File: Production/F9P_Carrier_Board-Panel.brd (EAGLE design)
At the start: 154.9 x 146.3 mm, 666 parts, among them J11 MICROMOD-2222-C, J13 U.FL, J14 QWIIC_RIGHT_ANGLE, J17 JTAG, J20 MICROMOD-2222-C, J22 U.FL, J23 QWIIC_RIGHT_ANGLE, J26 JTAG, J29 MICROMOD-2222-C, J31 U.FL, J32 QWIIC_RIGHT_ANGLE, J35 JTAG, J4 U.FL, J5 QWIIC_RIGHT_ANGLE, J6 MICROMOD-2222-C, J8 JTAG, U1 U-BLOX_ZED-F9P, U2 AP7361C-33, U3 U-BLOX_ZED-F9P, U4 AP7361C-33, U5 AP7361C-33, U6 U-BLOX_ZED-F9P, U7 AP7361C-33, U8 U-BLOX_ZED-F9P

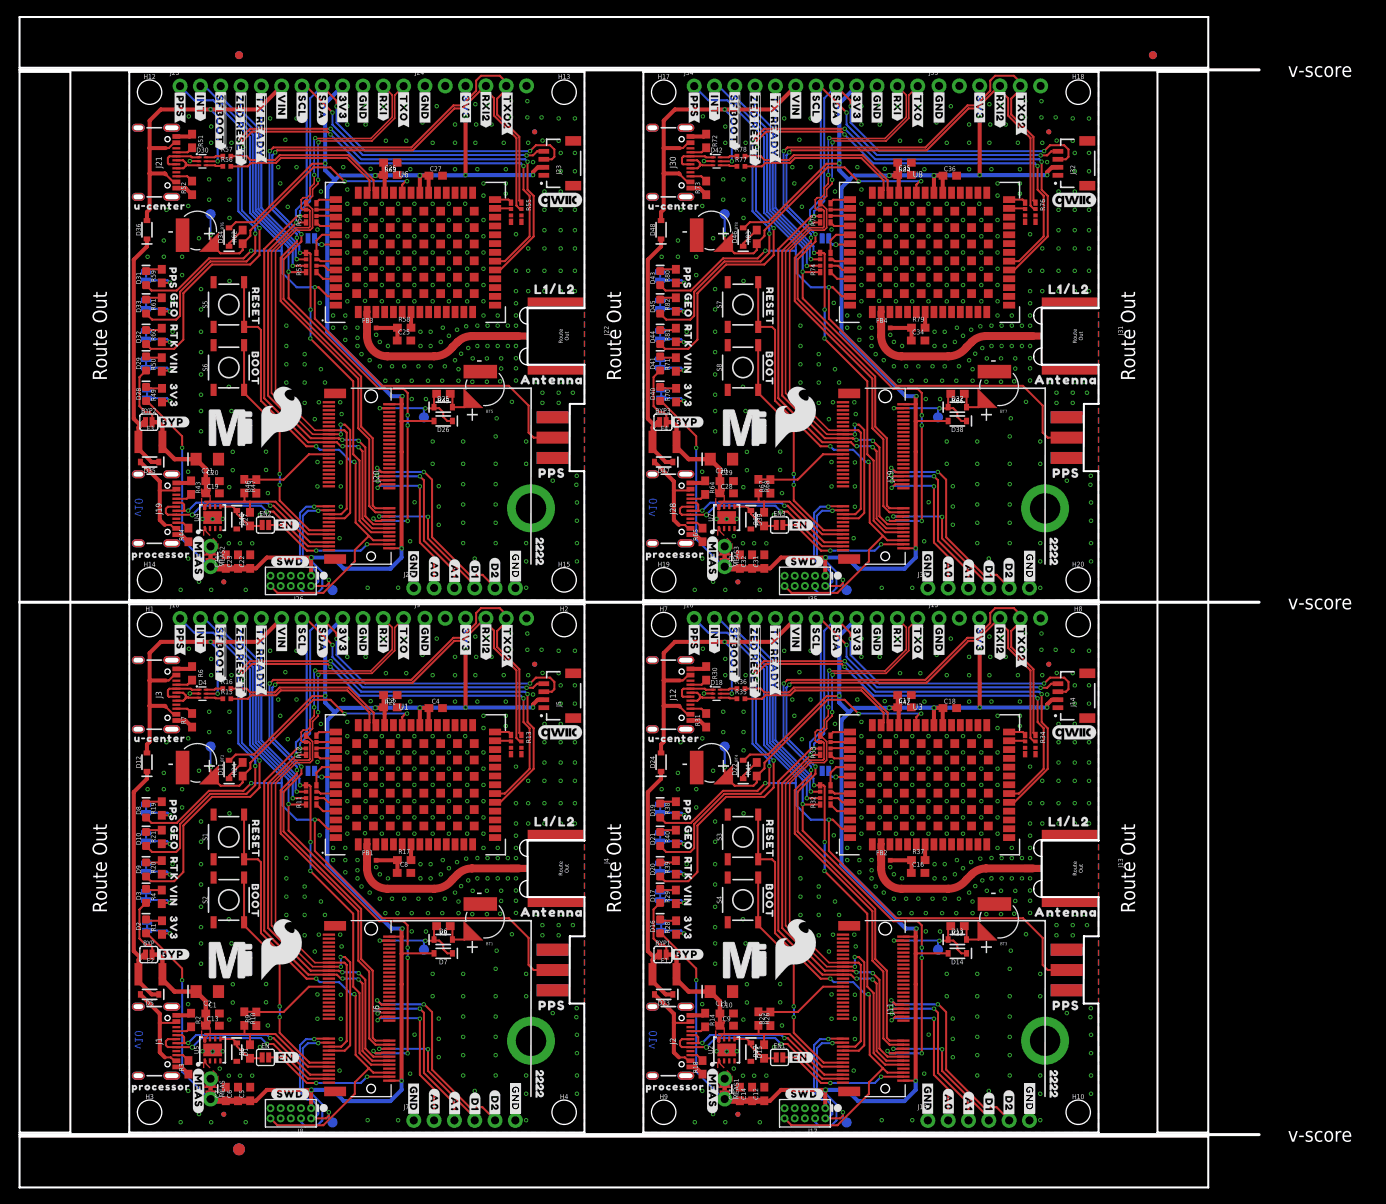
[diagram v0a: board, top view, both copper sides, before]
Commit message: Removes GPS silk, adds GNSS silk, repanelizes with new silk
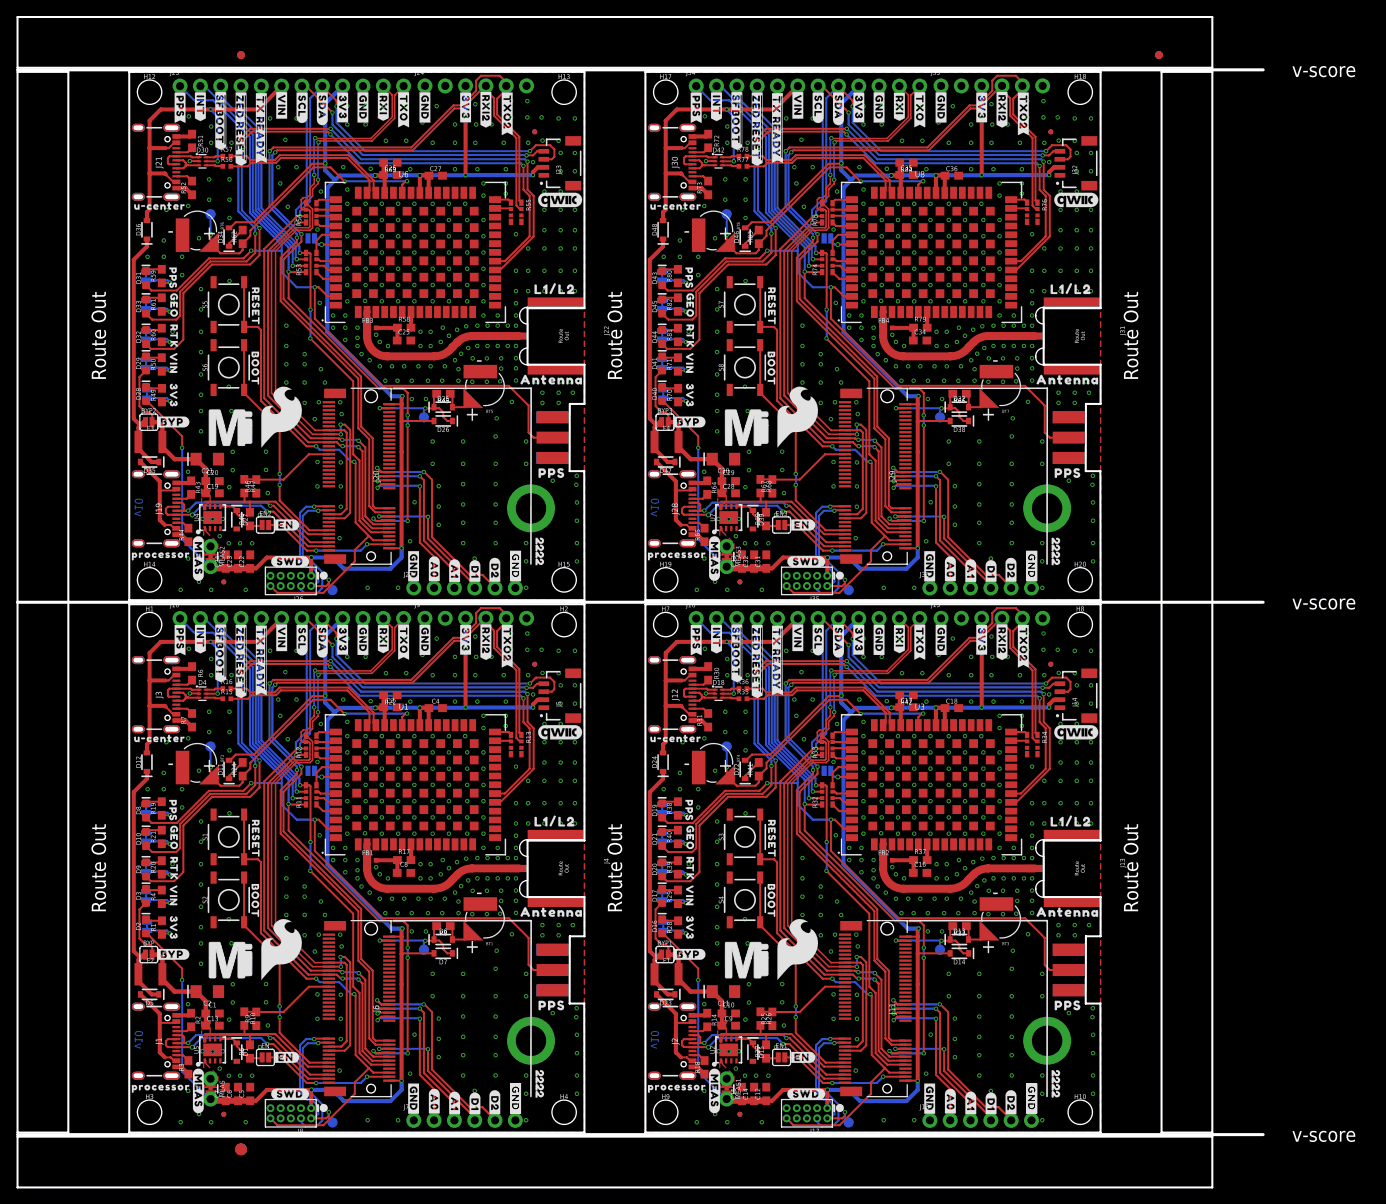
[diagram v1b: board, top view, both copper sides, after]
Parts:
- U$120, U$206, U$288: device top:GPS19 -> top:U#CENTER20
- U$121, U$207, U$289: device top:U#CENTER20 -> SparkFun-Aesthetics:QWIIC_5.5MM
- U$122, U$208, U$290: device SparkFun-Aesthetics:QWIIC_5.5MM -> bot:#SCL#1
- U$123, U$209, U$291: device bot:#SCL#1 -> bot:#SDA#0
- U$124, U$210, U$292: device bot:#SDA#0 -> bot:#TXO#5
- U$125, U$211, U$293: device bot:#TXO#5 -> bot:#RXI#6
- U$126, U$212, U$294: device bot:#RXI#6 -> top:PPS15
- U$127, U$213, U$295: device top:PPS15 -> top:ANTENNA16
- U$128, U$214, U$296: device top:ANTENNA16 -> top:L1#L216
- U$129, U$215, U$297: device top:L1#L216 -> top:##CS##9
- U$130, U$216, U$298: device top:##CS##9 -> top:#CLK#7
- U$135, U$217, U$299: device top:#CLK#7 -> top:#SDO#9
- U$136, U$218, U$300: device top:#SDO#9 -> top:#SDI#11
- U$137, U$219, U$301: device top:#SDI#11 -> top:BLUETOOTH24
- U$138, U$220, U$302: device top:BLUETOOTH24 -> top:U#CENTER22
- U$139, U$221, U$303: device top:U#CENTER22 -> top:L1#L217
- U$140, U$222, U$304: device top:L1#L217 -> top:ANTENNA17
- U$141, U$223, U$305: device top:ANTENNA17 -> top:PPS16
- U$142, U$224, U$306: device top:PPS16 -> bot:##ZED_RESET##9
- U$143, U$225, U$307: device bot:##ZED_RESET##9 -> top:##ZED_RESET##14
- U$144, U$226, U$308: device top:##ZED_RESET##14 -> top:##SFBOOT##13
- U$145, U$227, U$309: device top:##SFBOOT##13 -> bot:##SFBOOT##8
- U$146, U$228, U$310: device bot:##SFBOOT##8 -> SparkFun-MicroMod:MICROMOD_LOGO_.5
- U$147, U$229, U$311: device SparkFun-MicroMod:MICROMOD_LOGO_.5 -> SparkFun-MicroMod:MICROMOD_MI_LOGO_1
- U$148, U$230, U$312: device SparkFun-MicroMod:MICROMOD_MI_LOGO_1 -> SparkFun-Aesthetics:SFE_LOGO_FLAME_.3
- U$149, U$231, U$313: device SparkFun-Aesthetics:SFE_LOGO_FLAME_.3 -> top:#GND#0
- U$152, U$234, U$316: device top:#GND#0 -> top:#A0#8
- U$153, U$235, U$317: device top:#A0#8 -> top:#A1#8
- U$154, U$236, U$318: device top:#A1#8 -> top:#D1#8
- U$155, U$237, U$319: device top:#D1#8 -> top:#D2#8
- U$156, U$238, U$320: device top:#D2#8 -> top:PROCESSOR23
- U$158, U$240, U$322: device top:PROCESSOR23 -> bot:#A0#14
- U$159, U$241, U$323: device bot:#A0#14 -> bot:#A1#14
- U$160, U$242, U$324: device bot:#A1#14 -> bot:#D1#14
- U$161, U$243, U$325: device bot:#D1#14 -> bot:#D2#14
- U$162, U$244, U$326: device bot:#D2#14 -> top:#GND#0
- U$164, U$246, U$328: device top:#GND#0 -> top:GNSS21
- U$45: device top:GPS19 -> top:GNSS21
- moved U$224 54.7 mm to (14.0, 125.6), flipped to the top, turned to 270 degrees
- moved U$142 54.5 mm to (78.5, 59.1), flipped to the top, turned to 270 degrees
- moved U$306 54.5 mm to (78.5, 125.6), flipped to the top, turned to 270 degrees
- moved U$139 53.0 mm to (117.5, 38.2), turned to 0 degrees
- moved U$303 53.0 mm to (117.5, 104.8), turned to 0 degrees
- moved U$221 52.7 mm to (53.0, 104.8), turned to 0 degrees
- moved U$126 50.7 mm to (117.3, 15.9), turned to 0 degrees
- moved U$294 50.7 mm to (117.3, 82.4), turned to 0 degrees
- moved U$212 50.6 mm to (52.8, 82.4), turned to 0 degrees
- moved U$121 50.3 mm to (118.4, 50.0)
- moved U$289 50.3 mm to (118.4, 116.6)
- moved U$207 50.0 mm to (53.8, 116.6)
- moved U$238 41.8 mm to (3.96, 72.3), turned to 0 degrees
- moved U$156 41.5 mm to (68.5, 5.74), turned to 0 degrees
- moved U$320 41.5 mm to (68.5, 72.3), turned to 0 degrees
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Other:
- board size 154.9 x 146.3 mm -> 155.7 x 146.3 mm

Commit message: Updated panel
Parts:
- added D49: 0.5A/40V/420mV, SparkFun-DiscreteSemi:SOD-323
- added D50, D51: 3A/10V/280mV, SparkFun-DiscreteSemi:SOD-323
- added D52: PESD0402, SparkFun-DiscreteSemi:0402
- added U$329: (no value), bot:##SFBOOT##8
- added U$330: (no value), SparkFun-MicroMod:MICROMOD_LOGO_.5
- added U$331: (no value), SparkFun-MicroMod:MICROMOD_MI_LOGO_1
- added U$332: (no value), SparkFun-Aesthetics:SFE_LOGO_FLAME_.3
- added U$333, U$334, U$335, U$346, U$347: (no value), top:#GND#0
- added U$336: (no value), top:#A0#8
- added U$337: (no value), top:#A1#8
- added U$338: (no value), top:#D1#8
- added U$339: (no value), top:#D2#8
- added U$340, U$341: (no value), top:PROCESSOR23
- added U$342: (no value), bot:#A0#14
- added U$343: (no value), bot:#A1#14
- added U$344: (no value), bot:#D1#14
- added U$345: (no value), bot:#D2#14
- added U$348: (no value), top:GNSS21
- added U$349: (no value), top:GNSS501
- added U$350: (no value), top:CARRIER502
- added U$351: (no value), top:BOARD503
- added U$352: (no value), top:2222501
- added U$353, U$354: (no value), top:#NC#4
- added U$355, U$356: (no value), top:#NC#5
- D13: value 3A/10V/280mV -> PESD0402; device SparkFun-DiscreteSemi:SOD-323 -> SparkFun-DiscreteSemi:0402
- D14, D38: value 1A/23V/620mV -> 3A/10V/280mV
- D15: value 3.3V -> 1A/23V/620mV
- D16, D29: value RED -> 3.3V; device SparkFun-LED:LED-0603 -> SparkFun-DiscreteSemi:SOD-323
- D18, D30: value PRTR5V0U2F -> RED; device SparkFun-IC-Power:SOT886 -> SparkFun-LED:LED-0603
- D19, D32, D45: value BLUE -> PRTR5V0U2F; device SparkFun-LED:LED-0603 -> SparkFun-IC-Power:SOT886
- D22, D34, D46: value 0.5A/40V/420mV -> BLUE; device SparkFun-DiscreteSemi:SOD-323 -> SparkFun-LED:LED-0603
- D23, D36: value 3A/10V/280mV -> 0.5A/40V/420mV
- D26: value 1A/23V/620mV -> PESD0402; device SparkFun-DiscreteSemi:SOD-323 -> SparkFun-DiscreteSemi:0402
- D27: value 3.3V -> 3A/10V/280mV
- D28, D41: value RED -> 1A/23V/620mV; device SparkFun-LED:LED-0603 -> SparkFun-DiscreteSemi:SOD-323
- D31, D43, D44: value BLUE -> RED
- D35, D47, D48: value 3A/10V/280mV -> BLUE; device SparkFun-DiscreteSemi:SOD-323 -> SparkFun-LED:LED-0603
- D39: value 3.3V -> PESD0402; device SparkFun-DiscreteSemi:SOD-323 -> SparkFun-DiscreteSemi:0402
- D40: value RED -> 3A/10V/280mV; device SparkFun-LED:LED-0603 -> SparkFun-DiscreteSemi:SOD-323
- D42: value PRTR5V0U2F -> 3.3V; device SparkFun-IC-Power:SOT886 -> SparkFun-DiscreteSemi:SOD-323
- H11, H16, H5, H6: value STAND-OFF-REFLOW2.5MM_TALL -> STAND-OFF-REFLOW-M2.5_2.5MM_TALL
- J13, J22, J31, J4: device SparkFun-RF:SMA-EDGE-SMD -> SparkFun-RF:SMA-EDGE
- MEAS, MEAS1, MEAS2, MEAS3: value (none) -> JUMPER-COMBO_2_NC_TRACE
- U$100: device top:GEO15 -> top:#GND#0
- U$101: device top:PPS14 -> top:#GND#0
- U$102: device top:RTK16 -> top:#PPS#6
- U$103: device bot:#GEO#9 -> top:#RXI2#9
- U$104: device bot:#PPS#10 -> top:#TXO2#9
- U$105: device bot:#RTK#8 -> top:#VIN#13
- U$106: device bot:#SPI#11 -> top:GEO15
- U$107: device top:#3V3#1 -> top:PPS14
- U$108: device top:#3V3#1 -> top:RTK16
- U$109: device top:#GND#0 -> bot:#GEO#9
- U$110: device top:#GND#0 -> bot:#PPS#10
- U$111: device top:#VIN#13 -> bot:#RTK#8
- U$112: device top:#INT#10 -> bot:#SPI#11
- U$113, U$281: device top:##TX_READY##13 -> top:#3V3#1
- U$114: device bot:##TX_READY##7 -> top:#3V3#1
- U$115, U$283: device bot:#INT#4 -> top:#GND#0
- U$116: device bot:#PPS#3 -> top:#GND#0
- U$117: device bot:#TXO2#10 -> top:#VIN#13
- U$118: device bot:#RXI2#10 -> top:#INT#10
- U$119: device top:ZED#F9P19 -> top:##TX_READY##13
- U$120: device top:U#CENTER20 -> bot:##TX_READY##7
- U$121: device SparkFun-Aesthetics:QWIIC_5.5MM -> bot:#INT#4
- U$122: device bot:#SCL#1 -> bot:#PPS#3
- U$123: device bot:#SDA#0 -> bot:#TXO2#10
- U$124: device bot:#TXO#5 -> bot:#RXI2#10
- U$125: device bot:#RXI#6 -> top:ZED#F9P19
- U$126: device top:PPS15 -> top:U#CENTER20
- U$127: device top:ANTENNA16 -> SparkFun-Aesthetics:QWIIC_5.5MM
- U$128: device top:L1#L216 -> bot:#SCL#1
- U$129: device top:##CS##9 -> bot:#SDA#0
- U$130: device top:#CLK#7 -> bot:#TXO#5
- U$135: device top:#SDO#9 -> bot:#RXI#6
- U$136: device top:#SDI#11 -> top:PPS15
- U$137: device top:BLUETOOTH24 -> top:ANTENNA16
- U$138: device top:U#CENTER22 -> top:L1#L216
- U$139: device top:L1#L217 -> top:##CS##9
- U$140: device top:ANTENNA17 -> top:#CLK#7
- U$141: device top:PPS16 -> top:#SDO#9
- U$142: device bot:##ZED_RESET##9 -> top:#SDI#11
- U$143: device top:##ZED_RESET##14 -> top:BLUETOOTH24
- U$144: device top:##SFBOOT##13 -> top:U#CENTER22
- U$145: device bot:##SFBOOT##8 -> top:L1#L217
- U$146: device SparkFun-MicroMod:MICROMOD_LOGO_.5 -> top:ANTENNA17
- U$147: device SparkFun-MicroMod:MICROMOD_MI_LOGO_1 -> top:PPS16
- U$148: device SparkFun-Aesthetics:SFE_LOGO_FLAME_.3 -> bot:##ZED_RESET##9
- U$149, U$327: device top:#GND#0 -> top:##ZED_RESET##14
- U$150: device top:#GND#0 -> top:##SFBOOT##13
- U$151: device top:#GND#0 -> bot:##SFBOOT##8
- U$152: device top:#A0#8 -> SparkFun-MicroMod:MICROMOD_LOGO_.5
- U$153: device top:#A1#8 -> SparkFun-MicroMod:MICROMOD_MI_LOGO_1
- U$154: device top:#D1#8 -> SparkFun-Aesthetics:SFE_LOGO_FLAME_.3
- U$155: device top:#D2#8 -> top:#GND#0
- U$156, U$157: device top:PROCESSOR23 -> top:#GND#0
- U$158: device bot:#A0#14 -> top:#A0#8
- U$159: device bot:#A1#14 -> top:#A1#8
- U$160: device bot:#D1#14 -> top:#D1#8
- U$161: device bot:#D2#14 -> top:#D2#8
- U$162, U$163: device top:#GND#0 -> top:PROCESSOR23
- U$164: device top:GNSS21 -> bot:#A0#14
- U$165: device buzzard_labels (9):22229 -> bot:#A1#14
- U$166: device power:#BYP#8 -> bot:#D1#14
- U$167: device power:#RESET10 -> bot:#D2#14
- U$168: device power:BOOT10 -> top:#GND#0
- U$169: device power:#MEAS#10 -> top:#GND#0
- U$170: device power:#SWD#10 -> top:GNSS21
- U$171: device headers_dup:VIN3 -> top:GNSS501
- U$172: device headers_dup:3V34 -> top:CARRIER502
- U$173: device fl3:#SWD#10 -> top:BOARD503
- U$174: device fl3:#MEAS#10 -> top:2222501
- U$175: device fl3:#VIN_LED#10 -> top:#NC#4
- U$176: device fl3:#3V3_LED#10 -> top:#NC#4
- U$177: device output:#EN#0 -> top:#NC#5
- U$178: device top:#3V3#1 -> top:#NC#5
- U$179: device top:#3V3#1 -> power:#BYP#8
- U$180: device top:#GND#0 -> power:#RESET10
- U$181: device top:#GND#0 -> power:BOOT10
- U$182: device top:#PPS#6 -> power:#MEAS#10
- U$183: device top:#RXI2#9 -> power:#SWD#10
- U$184: device top:#TXO2#9 -> headers_dup:VIN3
- U$185: device top:#VIN#13 -> headers_dup:3V34
- U$186: device top:GEO15 -> fl3:#SWD#10
- U$187: device top:PPS14 -> fl3:#MEAS#10
- U$188: device top:RTK16 -> fl3:#VIN_LED#10
- U$189: device bot:#GEO#9 -> fl3:#3V3_LED#10
- U$190: device bot:#PPS#10 -> output:#EN#0
- U$191: device bot:#RTK#8 -> top:#3V3#1
- U$192: device bot:#SPI#11 -> top:#3V3#1
- U$193, U$194: device top:#3V3#1 -> top:#GND#0
- U$195: device top:#GND#0 -> top:#PPS#6
- U$196: device top:#GND#0 -> top:#RXI2#9
- U$197: device top:#VIN#13 -> top:#TXO2#9
- U$198: device top:#INT#10 -> top:#VIN#13
- U$199: device top:##TX_READY##13 -> top:GEO15
- U$200: device bot:##TX_READY##7 -> top:PPS14
- U$201: device bot:#INT#4 -> top:RTK16
- U$202: device bot:#PPS#3 -> bot:#GEO#9
- U$203: device bot:#TXO2#10 -> bot:#PPS#10
- U$204: device bot:#RXI2#10 -> bot:#RTK#8
- U$205: device top:ZED#F9P19 -> bot:#SPI#11
- U$206: device top:U#CENTER20 -> top:#3V3#1
- U$207: device SparkFun-Aesthetics:QWIIC_5.5MM -> top:#3V3#1
- U$208: device bot:#SCL#1 -> top:#GND#0
- U$209: device bot:#SDA#0 -> top:#GND#0
- U$210: device bot:#TXO#5 -> top:#VIN#13
- U$211: device bot:#RXI#6 -> top:#INT#10
- U$212: device top:PPS15 -> top:##TX_READY##13
- U$213: device top:ANTENNA16 -> bot:##TX_READY##7
- U$214: device top:L1#L216 -> bot:#INT#4
- U$215: device top:##CS##9 -> bot:#PPS#3
- U$216: device top:#CLK#7 -> bot:#TXO2#10
- U$217: device top:#SDO#9 -> bot:#RXI2#10
- U$218: device top:#SDI#11 -> top:ZED#F9P19
- U$219: device top:BLUETOOTH24 -> top:U#CENTER20
- U$220: device top:U#CENTER22 -> SparkFun-Aesthetics:QWIIC_5.5MM
- U$221: device top:L1#L217 -> bot:#SCL#1
- U$222: device top:ANTENNA17 -> bot:#SDA#0
- U$223: device top:PPS16 -> bot:#TXO#5
- U$224: device bot:##ZED_RESET##9 -> bot:#RXI#6
- U$225: device top:##ZED_RESET##14 -> top:PPS15
- U$226: device top:##SFBOOT##13 -> top:ANTENNA16
- U$227: device bot:##SFBOOT##8 -> top:L1#L216
- U$228: device SparkFun-MicroMod:MICROMOD_LOGO_.5 -> top:##CS##9
- U$229: device SparkFun-MicroMod:MICROMOD_MI_LOGO_1 -> top:#CLK#7
- U$230: device SparkFun-Aesthetics:SFE_LOGO_FLAME_.3 -> top:#SDO#9
- U$231: device top:#GND#0 -> top:#SDI#11
- U$232: device top:#GND#0 -> top:BLUETOOTH24
- U$233: device top:#GND#0 -> top:U#CENTER22
- U$234: device top:#A0#8 -> top:L1#L217
- U$235: device top:#A1#8 -> top:ANTENNA17
- U$236: device top:#D1#8 -> top:PPS16
- U$237: device top:#D2#8 -> bot:##ZED_RESET##9
- U$238: device top:PROCESSOR23 -> top:##ZED_RESET##14
- U$239: device top:PROCESSOR23 -> top:##SFBOOT##13
- U$240: device bot:#A0#14 -> bot:##SFBOOT##8
- U$241: device bot:#A1#14 -> SparkFun-MicroMod:MICROMOD_LOGO_.5
- U$242: device bot:#D1#14 -> SparkFun-MicroMod:MICROMOD_MI_LOGO_1
- U$243: device bot:#D2#14 -> SparkFun-Aesthetics:SFE_LOGO_FLAME_.3
- U$246: device top:GNSS21 -> top:#GND#0
- U$247: device buzzard_labels (9):22229 -> top:#A0#8
- U$248: device power:#BYP#8 -> top:#A1#8
- U$249: device power:#RESET10 -> top:#D1#8
- U$250: device power:BOOT10 -> top:#D2#8
- U$251: device power:#MEAS#10 -> top:PROCESSOR23
- U$252: device power:#SWD#10 -> top:PROCESSOR23
- U$253: device headers_dup:VIN3 -> bot:#A0#14
- U$254: device headers_dup:3V34 -> bot:#A1#14
- U$255: device fl3:#SWD#10 -> bot:#D1#14
- U$256: device fl3:#MEAS#10 -> bot:#D2#14
- U$257: device fl3:#VIN_LED#10 -> top:#GND#0
- U$258: device fl3:#3V3_LED#10 -> top:#GND#0
- U$259: device output:#EN#0 -> top:GNSS21
- U$260: device top:#3V3#1 -> top:GNSS501
- U$261: device top:#3V3#1 -> top:CARRIER502
- U$262: device top:#GND#0 -> top:BOARD503
- U$263: device top:#GND#0 -> top:2222501
- U$264: device top:#PPS#6 -> top:#NC#4
- U$265: device top:#RXI2#9 -> top:#NC#4
- U$266: device top:#TXO2#9 -> top:#NC#5
- U$267: device top:#VIN#13 -> top:#NC#5
- U$268: device top:GEO15 -> power:#BYP#8
- U$269: device top:PPS14 -> power:#RESET10
- U$270: device top:RTK16 -> power:BOOT10
- U$271: device bot:#GEO#9 -> power:#MEAS#10
- U$272: device bot:#PPS#10 -> power:#SWD#10
- U$273: device bot:#RTK#8 -> headers_dup:VIN3
- U$274: device bot:#SPI#11 -> headers_dup:3V34
- U$275, U$93: device top:#3V3#1 -> fl3:#SWD#10
- U$276: device top:#3V3#1 -> fl3:#MEAS#10
- U$277, U$95: device top:#GND#0 -> fl3:#VIN_LED#10
- U$278: device top:#GND#0 -> fl3:#3V3_LED#10
- U$279: device top:#VIN#13 -> output:#EN#0
- U$280: device top:#INT#10 -> top:#3V3#1
- U$282: device bot:##TX_READY##7 -> top:#GND#0
- U$284: device bot:#PPS#3 -> top:#PPS#6
- U$285: device bot:#TXO2#10 -> top:#RXI2#9
- U$286: device bot:#RXI2#10 -> top:#TXO2#9
- U$287: device top:ZED#F9P19 -> top:#VIN#13
- U$288: device top:U#CENTER20 -> top:GEO15
- U$289: device SparkFun-Aesthetics:QWIIC_5.5MM -> top:PPS14
- U$290: device bot:#SCL#1 -> top:RTK16
- U$291: device bot:#SDA#0 -> bot:#GEO#9
- U$292: device bot:#TXO#5 -> bot:#PPS#10
- U$293: device bot:#RXI#6 -> bot:#RTK#8
- U$294: device top:PPS15 -> bot:#SPI#11
- U$295: device top:ANTENNA16 -> top:#3V3#1
- U$296: device top:L1#L216 -> top:#3V3#1
- U$297: device top:##CS##9 -> top:#GND#0
- U$298: device top:#CLK#7 -> top:#GND#0
- U$299: device top:#SDO#9 -> top:#VIN#13
- U$300: device top:#SDI#11 -> top:#INT#10
- U$301: device top:BLUETOOTH24 -> top:##TX_READY##13
- U$302: device top:U#CENTER22 -> bot:##TX_READY##7
- U$303: device top:L1#L217 -> bot:#INT#4
- U$304: device top:ANTENNA17 -> bot:#PPS#3
- U$305: device top:PPS16 -> bot:#TXO2#10
- U$306: device bot:##ZED_RESET##9 -> bot:#RXI2#10
- U$307: device top:##ZED_RESET##14 -> top:ZED#F9P19
- U$308: device top:##SFBOOT##13 -> top:U#CENTER20
- U$309: device bot:##SFBOOT##8 -> SparkFun-Aesthetics:QWIIC_5.5MM
- U$310: device SparkFun-MicroMod:MICROMOD_LOGO_.5 -> bot:#SCL#1
- U$311: device SparkFun-MicroMod:MICROMOD_MI_LOGO_1 -> bot:#SDA#0
- U$312: device SparkFun-Aesthetics:SFE_LOGO_FLAME_.3 -> bot:#TXO#5
- U$313: device top:#GND#0 -> bot:#RXI#6
- U$314: device top:#GND#0 -> top:PPS15
- U$315: device top:#GND#0 -> top:ANTENNA16
- U$316: device top:#A0#8 -> top:L1#L216
- U$317: device top:#A1#8 -> top:##CS##9
- U$318: device top:#D1#8 -> top:#CLK#7
- U$319: device top:#D2#8 -> top:#SDO#9
- U$320: device top:PROCESSOR23 -> top:#SDI#11
- U$321: device top:PROCESSOR23 -> top:BLUETOOTH24
- U$322: device bot:#A0#14 -> top:U#CENTER22
- U$323: device bot:#A1#14 -> top:L1#L217
- U$324: device bot:#D1#14 -> top:ANTENNA17
- U$325: device bot:#D2#14 -> top:PPS16
- U$326: device top:#GND#0 -> bot:##ZED_RESET##9
- U$328: device top:GNSS21 -> top:##SFBOOT##13
- U$55: device buzzard_labels (9):22229 -> top:#NC#4
- U$79: device buzzard_labels (9):22229 -> top:GNSS501
- U$80: device power:#BYP#8 -> top:CARRIER502
- U$81: device power:#RESET10 -> top:BOARD503
- U$82: device power:BOOT10 -> top:2222501
- U$83: device power:#MEAS#10 -> top:#NC#4
- U$84: device power:#SWD#10 -> top:#NC#5
- U$85: device headers_dup:VIN3 -> top:#NC#5
- U$86: device headers_dup:3V34 -> power:#BYP#8
- U$87: device fl3:#SWD#10 -> power:#RESET10
- U$88: device fl3:#MEAS#10 -> power:BOOT10
- U$89: device fl3:#VIN_LED#10 -> power:#MEAS#10
- U$90: device fl3:#3V3_LED#10 -> power:#SWD#10
- U$91: device output:#EN#0 -> headers_dup:VIN3
- U$92: device top:#3V3#1 -> headers_dup:3V34
- U$94: device top:#GND#0 -> fl3:#MEAS#10
- U$96: device top:#PPS#6 -> fl3:#3V3_LED#10
- U$97: device top:#RXI2#9 -> output:#EN#0
- U$98: device top:#TXO2#9 -> top:#3V3#1
- U$99: device top:#VIN#13 -> top:#3V3#1
- moved U$167 137.0 mm to (110.0, 3.63), flipped to the bottom, turned to 90 degrees
- moved U$166 133.1 mm to (107.5, 3.48), flipped to the bottom, turned to 90 degrees
- moved U$168 133.0 mm to (112.5, 4.24), flipped to the bottom, turned to 90 degrees
- moved U$174 125.4 mm to (115.6, 6.35), flipped to the top, turned to 270 degrees
- moved U$169 123.9 mm to (112.5, 4.24)
- moved U$176 111.4 mm to (113.8, 62.0), flipped to the top, turned to 270 degrees
- moved U$79 106.0 mm to (21.5, 57.1), turned to 0 degrees
- moved D38 104.3 mm to (2.21, 112.9), turned to 90 degrees
- moved U$175 103.1 mm to (103.7, 62.1), flipped to the top, turned to 270 degrees
- moved D37 101.5 mm to (2.54, 83.8), turned to 180 degrees
- moved U$178 97.6 mm to (113.8, 62.0)
- moved U$172 95.3 mm to (94.2, 57.3), turned to 0 degrees
- moved U$170 90.8 mm to (99.8, 27.9), flipped to the bottom
- moved U$165 89.6 mm to (104.9, 3.53), flipped to the bottom, turned to 90 degrees
- moved D26 89.3 mm to (108.3, 32.4), turned to 90 degrees
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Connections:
- net 3.3V1: now also D15.A, D17.A, D23.A; no longer D14.A, D16.A, D22.A
- net 3.3V2: now also D30.A, D36.A; no longer D26.A, D34.A
- net 3.3V3: now also D41.A, D43.A, D49.A; no longer D38.A, D40.A, D46.A
- net 3.3V_EN1: now also D16.C; no longer D15.C
- net 3.3V_EN2: now also D29.C; no longer D27.C
- net 3.3V_EN3: now also D42.C; no longer D39.C
- net GEO_STAT1: now also D22.A; no longer D21.A
- net GEO_STAT2: now also D35.A; no longer D33.A
- net GEO_STAT3: now also D48.A; no longer D45.A
- net GND: now also D13.1, J4.GND@2, J4.GND@3
- net GND1: now also D16.A, D19.2, D26.1, J13.GND@2, J13.GND@3; no longer D15.A, D18.2
- net GND2: now also D29.A, D32.2, D39.1, J22.GND@2, J22.GND@3; no longer D27.A, D30.2
- net GND3: now also D42.A, D45.2, D52.1, J31.GND@2, J31.GND@3; no longer D39.A, D42.2
- net N$103: now also D45.3; no longer D42.3
- net N$104: now also D45.1; no longer D42.1
- net N$110: now also D46.C; no longer D43.C
- net N$111: now also D47.C; no longer D44.C
- net N$113: now also D48.C; no longer D45.C
- net N$114: now also D49.C; no longer D46.C
- net N$115: now also D43.C; no longer D40.C
- net N$118: now also D44.C; no longer D41.C
- net N$127: now also D45.6; no longer D42.6
- net N$128: now also D45.4; no longer D42.4
- net N$33: now also D14.A; no longer D13.A
- net N$37: now also D19.3; no longer D18.3
- net N$38: now also D19.1; no longer D18.1
- net N$44: now also D20.C; no longer D19.C
- net N$47: now also D21.C; no longer D20.C
- net N$49: now also D22.C; no longer D21.C
- net N$50: now also D23.C; no longer D22.C
- net N$51: now also D17.C; no longer D16.C
- net N$54: now also D18.C; no longer D17.C
- net N$63: now also D19.6; no longer D18.6
- net N$64: now also D19.4; no longer D18.4
- net N$67: now also D27.A; no longer D25.A
- net N$71: now also D32.3; no longer D30.3
- net N$72: now also D32.1; no longer D30.1
- net N$78: now also D33.C; no longer D31.C
- net N$79: now also D34.C; no longer D32.C
- net N$81: now also D35.C; no longer D33.C
- net N$82: now also D36.C; no longer D34.C
- net N$83: now also D30.C; no longer D28.C
- net N$86: now also D31.C; no longer D29.C
- net N$95: now also D32.6; no longer D30.6
- net N$96: now also D32.4; no longer D30.4
- net N$99: now also D40.A; no longer D37.A
- net PPS1: now also D20.A; no longer D19.A
- net PPS2: now also D33.A; no longer D31.A
- net PPS3: now also D46.A; no longer D43.A
- net RF_IN: now also D13.2
- net RF_IN1: now also D26.2
- net RF_IN2: now also D39.2
- net RF_IN3: now also D52.2
- net RTC_3V: now also TP1.1; no longer TP1.P$1
- net RTC_3V1: now also D15.C, TP4.1; no longer D13.C, TP4.P$1
- net RTC_3V2: now also D27.C, D28.C, TP7.1; no longer D25.C, D26.C, TP7.P$1
- net RTC_3V3: now also D40.C, D41.C, TP10.1; no longer D37.C, D38.C, TP10.P$1
- net RTK_STAT1: now also D21.A; no longer D20.A
- net RTK_STAT2: now also D34.A; no longer D32.A
- net RTK_STAT3: now also D47.A; no longer D44.A
- net SWDIO: now also TP2.1; no longer TP2.P$1
- net SWDIO1: now also TP5.1; no longer TP5.P$1
- net SWDIO2: now also TP8.1; no longer TP8.P$1
- net SWDIO3: now also TP11.1; no longer TP11.P$1
- net VIN1: now also D18.A; no longer D17.A
- net VIN2: now also D31.A; no longer D29.A
- net VIN3: now also D44.A; no longer D41.A
- net V_BATT: now also TP3.1; no longer TP3.P$1
- net V_BATT1: now also TP6.1; no longer TP6.P$1
- net V_BATT2: now also TP9.1; no longer TP9.P$1
- net V_BATT3: now also TP12.1; no longer TP12.P$1
- net V_FUSE1: now also D25.C; no longer D23.C
- net V_FUSE2: now also D37.C, D38.C; no longer D35.C, D36.C
- net V_FUSE3: now also D50.C, D51.C; no longer D47.C, D48.C
- net V_USB1: now also D24.A; no longer D23.A
- net V_USB2: now also D37.A; no longer D35.A
- net V_USB3: now also D50.A; no longer D47.A
- net V_USB_1: now also D19.5, D25.A; no longer D18.5, D24.A
- net V_USB_3: now also D32.5, D38.A; no longer D30.5, D36.A
- net V_USB_4: now also D45.5, D51.A; no longer D42.5, D48.A
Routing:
- net RF_IN2: track 22.5 -> 35.5 mm
- net RF_IN: track 22.5 -> 35.5 mm
- net RF_IN3: track 22.5 -> 35.5 mm
- net RF_IN1: track 22.5 -> 35.5 mm
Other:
- board size 155.7 x 146.3 mm -> 154.9 x 146.3 mm
